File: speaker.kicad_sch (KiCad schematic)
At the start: 18 parts, among them SW1 SW_DIP_x08

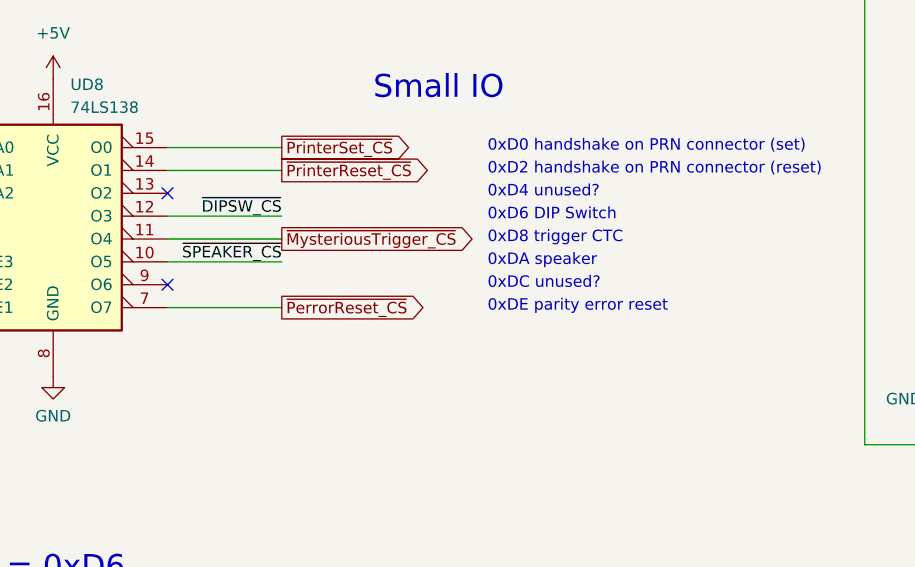
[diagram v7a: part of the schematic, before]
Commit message: FDC: added missing TC wire from small IO to FDC
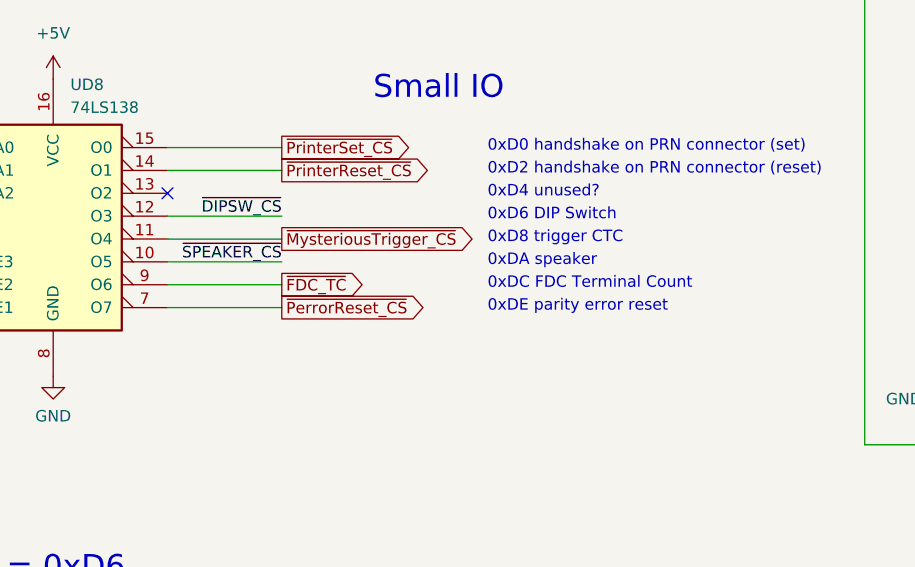
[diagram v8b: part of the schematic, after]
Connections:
- net ~{FDC_TC}: now reaches UD8.9 (O6)
- no-connect marks 4 -> 3
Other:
- note added: "0xDC FDC Terminal Count"
- note removed: "0xDC unused?"
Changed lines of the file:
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@@
   (no_connect (at 90.17 50.8))
   (no_connect (at 90.17 86.36))
-  (no_connect (at 90.17 96.52))
   (bus_entry (at 106.68 151.13) (size 2.54 2.54)
     (stroke (width 0) (type default))
@@
   )
   (wire (pts (xy 219.71 128.27) (xy 219.71 114.3))
+    (stroke (width 0) (type default))
+  )
+  (wire (pts (xy 102.87 96.52) (xy 90.17 96.52))
     (stroke (width 0) (type default))
   )
@@
     (effects (font (size 2.54 2.54)) (justify left bottom))
   )
-  (text "0xDC unused?" (at 125.73 97.155 0)
+  (text "0xDC FDC Terminal Count" (at 125.73 97.155 0)
     (effects (font (size 1.27 1.27)) (justify left bottom))
   )
@@
       (effects (font (size 1.27 1.27)) (justify left) hide)
     )
+  )
+  (global_label "~{FDC_TC}" (shape output) (at 102.87 96.52 0) (fields_autoplaced)
+    (effects (font (size 1.27 1.27)) (justify left))
+    (property "Intersheetrefs" "${INTERSHEET_REFS}" (at 112.689 96.52 0)
+      (effects (font (size 1.27 1.27)) (justify left) hide)
+    )
